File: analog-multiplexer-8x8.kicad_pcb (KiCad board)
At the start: 2 copper layers, 60.8 x 106.6 mm, 30 parts, among them J1 Conn_01x13, J2 Conn_02x08_Odd_Even, U1 4051, U2 4051, U3 4051, U4 4051, U5 4051, U6 4051, U7 4051, U8 4051

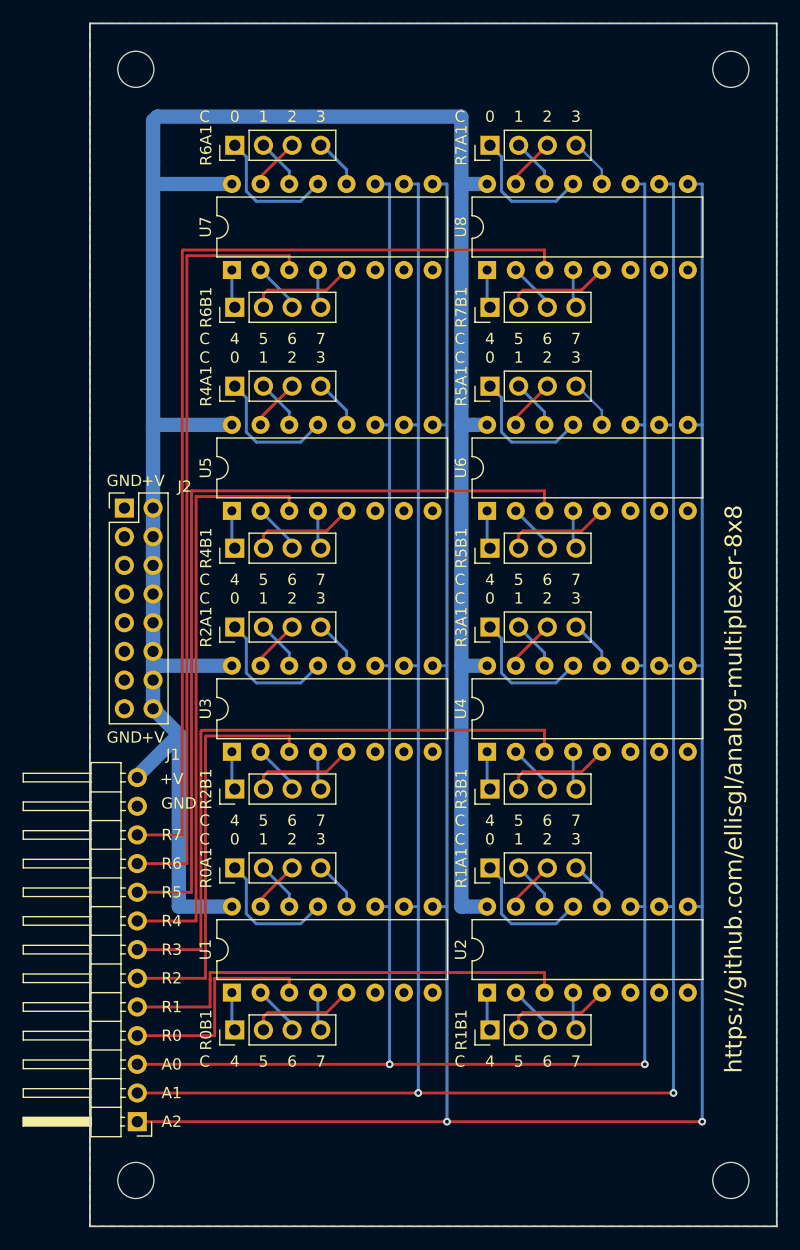
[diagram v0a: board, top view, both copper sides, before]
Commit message: Shrunk PCB to under 100mm
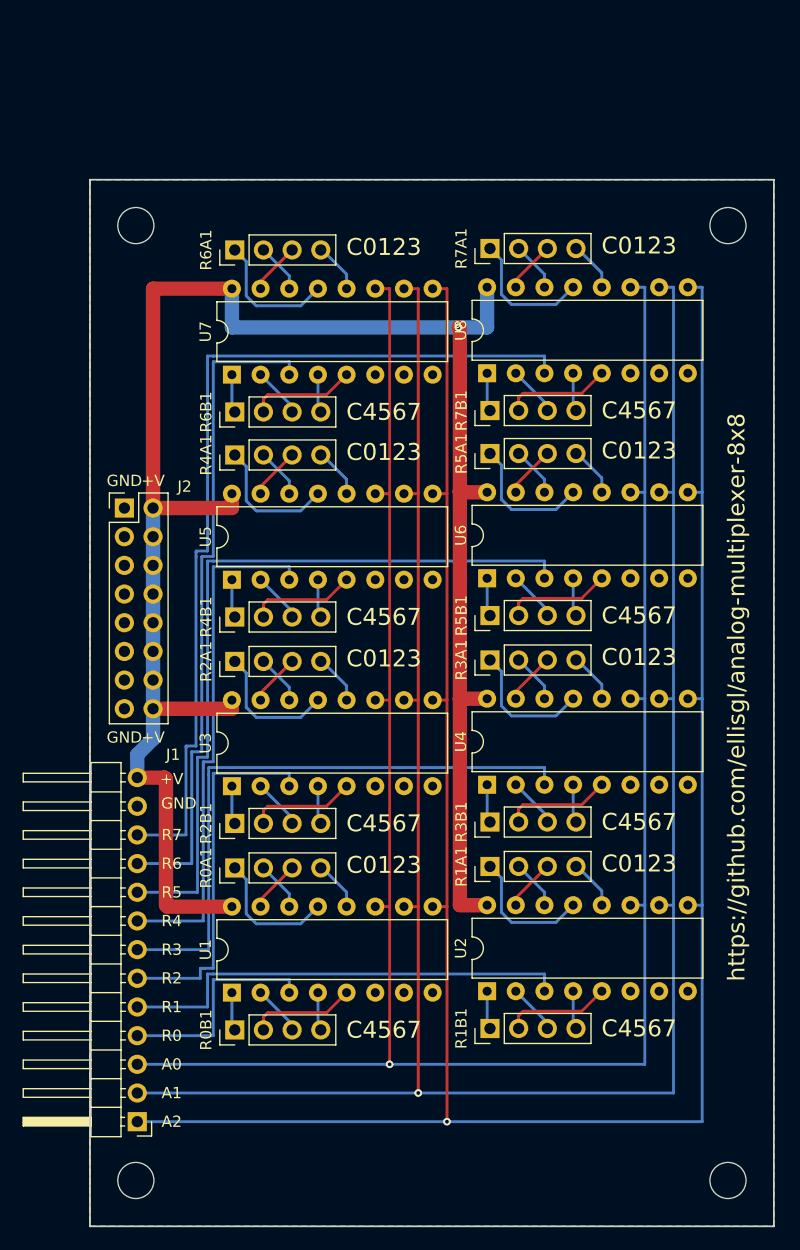
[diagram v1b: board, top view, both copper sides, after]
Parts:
- moved ? 13.8 mm to (80.8, 49.9)
- moved ? 13.8 mm to (28.3, 49.9)
- moved R6B1 9.27 mm to (37.1, 66.4)
- moved R6A1 9.27 mm to (37.1, 52.1)
- moved U7 9.27 mm to (36.8, 63.1)
- moved R7A1 9.14 mm to (59.7, 51.9)
- moved R7B1 9.14 mm to (59.7, 66.3)
- moved U8 9.14 mm to (59.4, 63.0)
- moved U5 6.10 mm to (36.8, 81.3)
- moved R4A1 6.10 mm to (37.1, 70.2)
- moved R4B1 6.10 mm to (37.1, 84.6)
- moved U6 5.97 mm to (59.4, 81.2)
- moved R5A1 5.97 mm to (59.7, 70.1)
- moved R5B1 5.97 mm to (59.7, 84.5)
- moved R2A1 3.05 mm to (37.1, 88.5)
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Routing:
- net A2: track 393.7 -> 207.9 mm, vias 2 -> 1
- net A1: track 381.0 -> 200.3 mm, vias 2 -> 1
- net A0: track 368.3 -> 192.7 mm, vias 2 -> 1
- net VCC: track 211.7 -> 175.3 mm, vias 0 -> 1
- net R7: track 89.6 -> 80.0 mm
- net R6: track 68.6 -> 59.0 mm
- net R5: track 73.4 -> 66.9 mm
- net R4: track 52.3 -> 46.0 mm
- net R3: track 57.4 -> 53.7 mm
- net R2: track 36.3 -> 32.8 mm
- net Net-(R5A1-Pad4): track 4.45 -> 7.63 mm
- net Net-(R7A1-Pad4): track 4.45 -> 7.63 mm
- net Net-(R1A1-Pad4): track 8.77 -> 7.63 mm
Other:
- board size 60.8 x 106.6 mm -> 60.6 x 92.7 mm
- board text added: "C0123"
- board text added: "C4567"
- board text removed: "0"
- board text removed: "1"
- board text removed: "2"
- board text removed: "3"
- board text removed: "4"
- board text removed: "5"
- board text removed: "6"
- board text removed: "7"
- board text removed: "C"

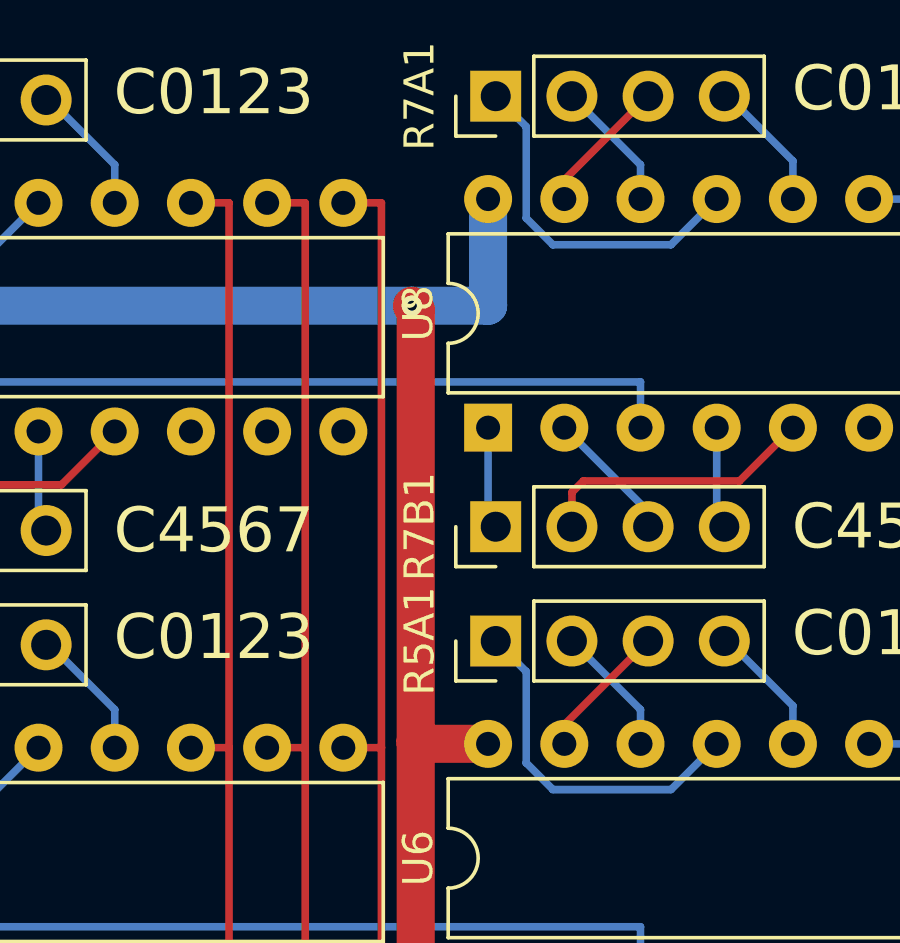
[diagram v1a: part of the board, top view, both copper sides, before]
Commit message: Removed via on power trace and re-used through-hole pin hole. 4 vias placed on the board, 4 vias places on the board, take one out, pass it around, 3 vias left on the board.
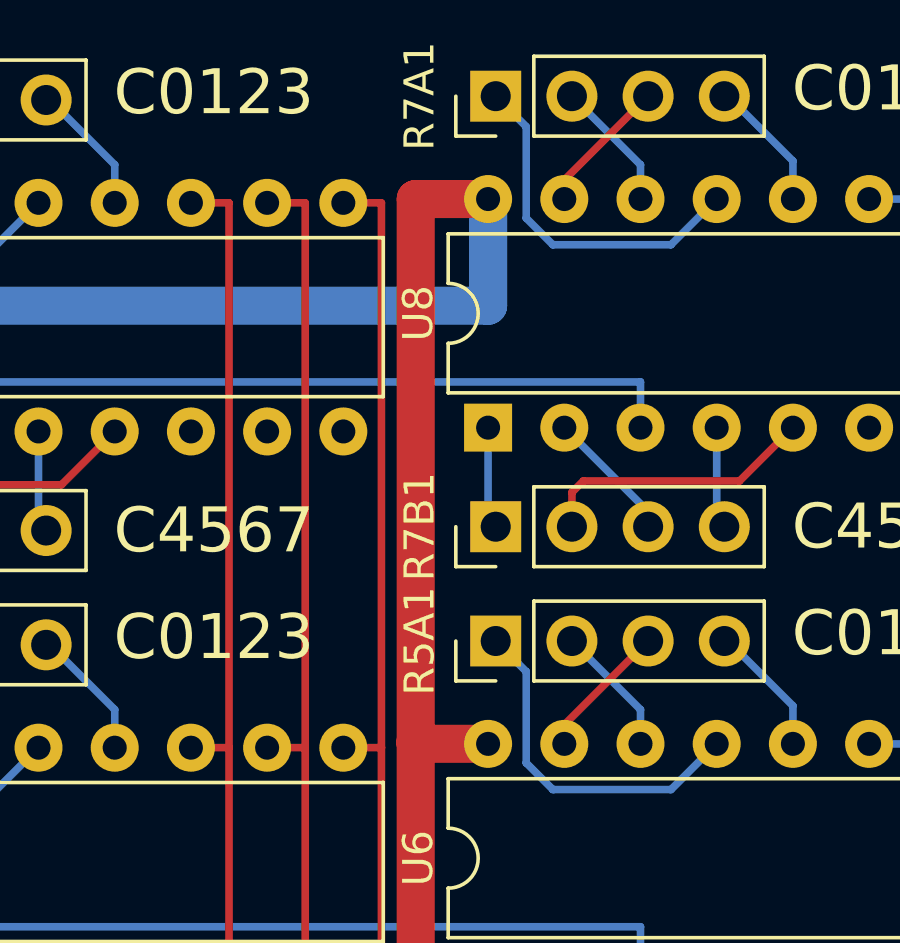
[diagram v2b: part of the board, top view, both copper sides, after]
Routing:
- net VCC: track 175.3 -> 181.3 mm, vias 1 -> 0
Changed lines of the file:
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@@
     (links 144)
     (no_connects 0)
-    (area 24.181999 45.771999 84.911001 138.632001)
+    (area 12.121287 45.771999 96.623 153.115001)
     (thickness 1.6)
     (drawings 45)
-    (tracks 445)
+    (tracks 444)
     (zones 0)
     (modules 30)
@@
   (segment (start 67.056 66.04) (end 67.31 66.294) (width 0.254) (layer B.Cu) (net 76) (status 30))
   (segment (start 67.056 66.04) (end 67.31 66.294) (width 0.2032) (layer B.Cu) (net 76) (status 30))
+  (segment (start 57.023 73.533) (end 57.023 55.372) (width 1.27) (layer F.Cu) (net 77))
+  (segment (start 57.023 55.372) (end 59.436 55.372) (width 1.27) (layer F.Cu) (net 77) (status 800000))
   (segment (start 59.436 73.533) (end 57.023 73.533) (width 1.27) (layer F.Cu) (net 77))
   (segment (start 57.277 73.406) (end 57.023 73.406) (width 1.27) (layer F.Cu) (net 77))
@@
   (segment (start 59.436 110.109) (end 57.023 110.109) (width 1.27) (layer F.Cu) (net 77))
   (segment (start 59.436 91.821) (end 57.023 91.821) (width 1.27) (layer F.Cu) (net 77))
-  (via (at 56.896 58.928) (size 0.6858) (drill 0.3302) (layers F.Cu B.Cu) (net 77))
   (segment (start 57.023 110.109) (end 57.023 110.109) (width 1.27) (layer F.Cu) (net 77))
   (segment (start 57.023 110.109) (end 57.023 91.821) (width 1.27) (layer F.Cu) (net 77))
   (segment (start 57.023 91.821) (end 57.023 73.406) (width 1.27) (layer F.Cu) (net 77))
-  (segment (start 57.023 73.406) (end 57.023 59.055) (width 1.27) (layer F.Cu) (net 77))
-  (segment (start 57.023 59.055) (end 56.896 58.928) (width 1.27) (layer F.Cu) (net 77))
   (segment (start 36.83 110.236) (end 31.115 110.236) (width 1.27) (layer F.Cu) (net 77))
   (segment (start 30.861 98.806) (end 28.448 98.806) (width 1.27) (layer F.Cu) (net 77))
@@
   (segment (start 36.83 74.93) (end 36.83 73.66) (width 1.27) (layer F.Cu) (net 77))
   (segment (start 59.436 55.372) (end 59.436 58.928) (width 1.27) (layer B.Cu) (net 77))
+  (segment (start 56.896 58.928) (end 36.83 58.928) (width 1.27) (layer B.Cu) (net 77))
+  (segment (start 59.436 58.928) (end 56.896 58.928) (width 1.27) (layer B.Cu) (net 77))
   (segment (start 36.83 58.928) (end 36.83 55.499) (width 1.27) (layer B.Cu) (net 77))
-  (segment (start 59.436 58.928) (end 56.896 58.928) (width 1.27) (layer B.Cu) (net 77))
-  (segment (start 56.896 58.928) (end 36.83 58.928) (width 1.27) (layer B.Cu) (net 77))
   (segment (start 29.845 74.93) (end 29.845 55.499) (width 1.27) (layer F.Cu) (net 77))
   (segment (start 29.845 55.499) (end 36.83 55.499) (width 1.27) (layer F.Cu) (net 77))
